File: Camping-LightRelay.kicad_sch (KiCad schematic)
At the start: 60 parts, among them CN1 U262-061N-4BVC11, CN2 XHP-2, CN3 B2B-XH-A, CN4 907-152A1022D10200, CN5 907-152A1022D10200, J1 J300, J2 J300, J3 J300, J4 J300, Q1 IRF7404, Q2 BC847, U1 LMV358ID

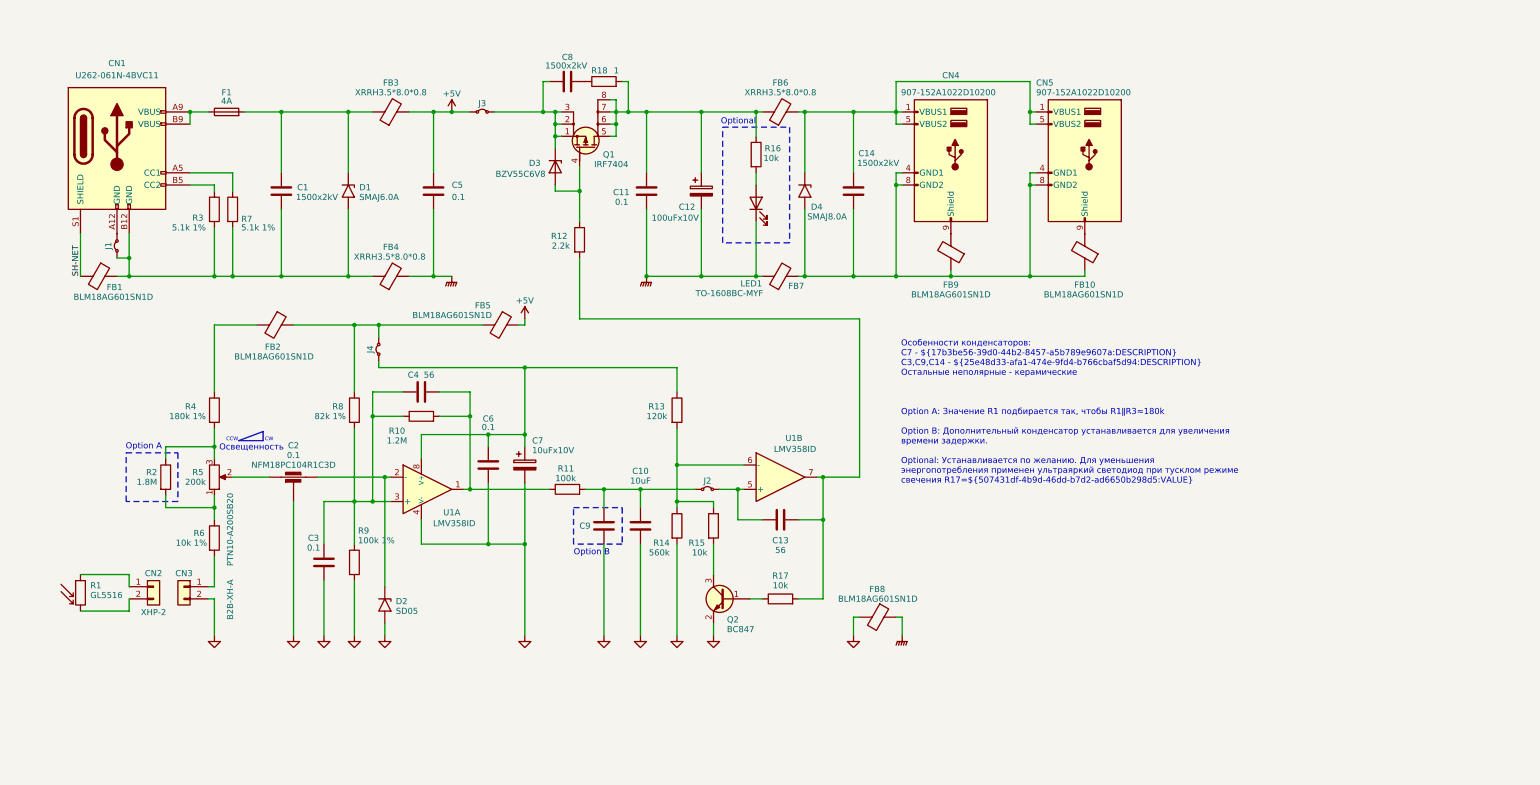
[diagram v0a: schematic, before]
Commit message: Отрисовка субмодуля управления питанием
Принципиальная схема (KiCAD) субмодуля управления PowerBank-ом. Создание электронных компонентов в базе. Выбор и назначение посадочных мест.
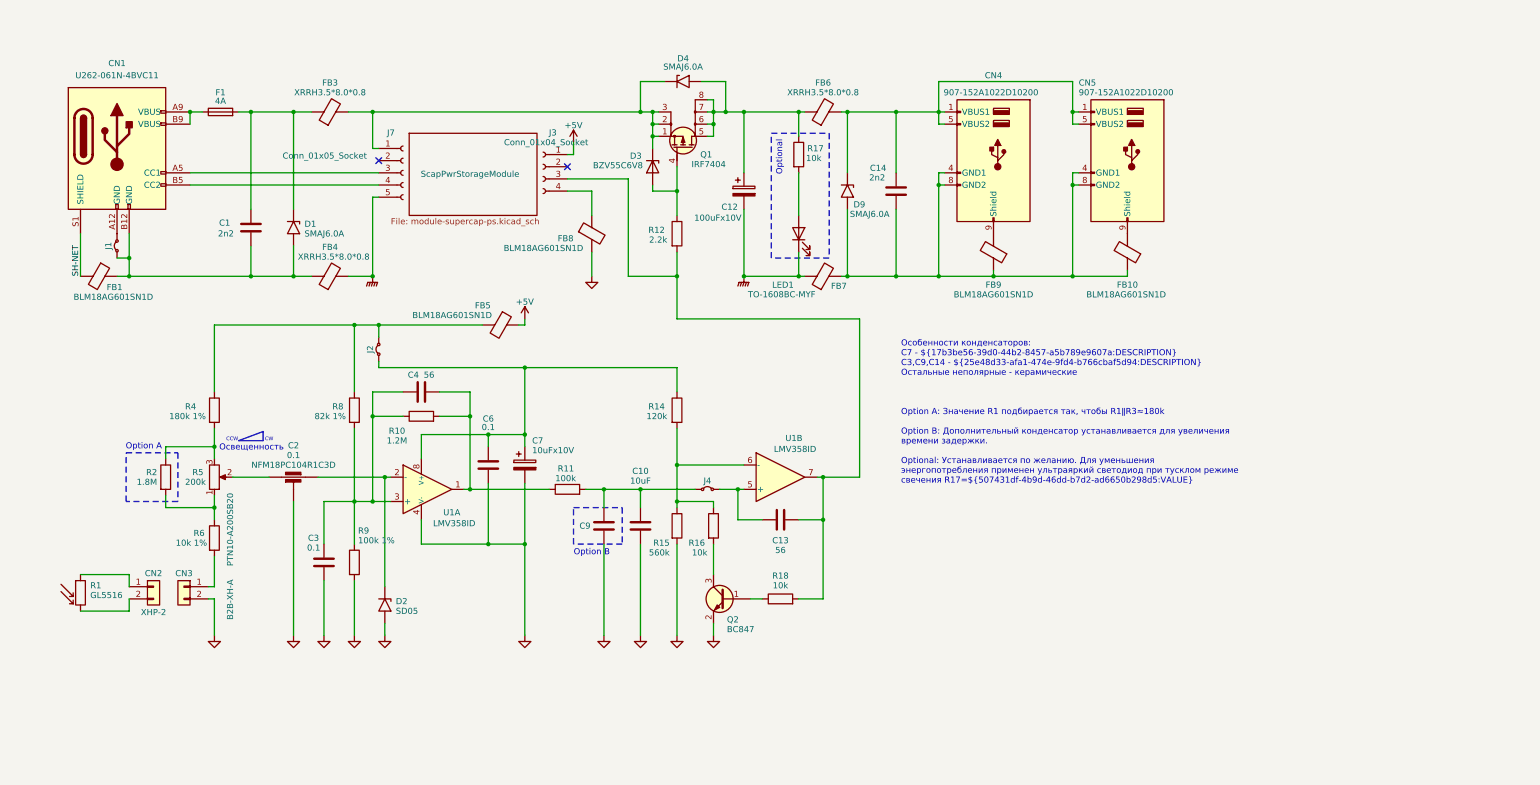
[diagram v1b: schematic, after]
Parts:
- removed C11, C5: 0.1, Capacitor_SMD:C_0603_1608Metric, symbol Device:C
- removed C8: 1500x2kV, Capacitor_THT:C_Disc_D7.5mm_W5.0mm_P5.00mm, symbol Device:C
- removed D4: SMAJ8.0A, Diode_SMD:D_SMA, symbol Diode:SMAJ8.0A
- removed FB2: BLM18AG601SN1D, Inductor_SMD:L_0603_1608Metric, symbol Device:FerriteBead
- removed J3: J300, lib:Junction_850mil, symbol Jumper:Jumper_2_Small_Bridged
- removed R18: 1, Resistor_SMD:R_0603_1608Metric, symbol Device:R
- removed R3, R7: 5.1k 1%, Resistor_SMD:R_0603_1608Metric, symbol Device:R
- added D4, D9: SMAJ6.0A, Diode_SMD:D_SMA, symbol Diode:SMAJ6.0A
- added J3: Conn_01x04_Socket, symbol Connector:Conn_01x04_Socket
- added J7: Conn_01x05_Socket, symbol Connector:Conn_01x05_Socket
- C1, C14: value 1500x2kV -> 2n2; footprint Capacitor_THT:C_Disc_D7.5mm_W5.0mm_P5.00mm -> Capacitor_THT:C_Disc_D8.0mm_W5.0mm_P7.50mm; Part Number (none) -> CY2222MD1PEE47J2A8
- C12: footprint Capacitor_THT:CP_Radial_D5.0mm_P2.50mm -> Capacitor_Tantalum_SMD:CP_EIA-3528-15_AVX-H_Pad1.50x2.35mm_HandSolder; Part Number (none) -> CA45-B010K107T
- C7: Part Number (none) -> TC212A106K010Y
- renumbered J4 to J2, J2 to J4, R13 to R14, R14 to R15, R15 to R16, R16 to R17, R17 to R18
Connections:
- net +5V: now also J3.1 (Pin_1); no longer FB3.2
- net GNDE: now also J7.5 (Pin_5); no longer FB8.1
- net at C14.1, CN4.1 (VBUS1), CN4.5 (VBUS2)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: now also D9.1 (A1)
- net at C14.2, CN4.4 (GND1), CN4.8 (GND2)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: now also D9.2 (A2)
- net at CN1.B5 (CC2): now also J7.4 (Pin_4)
- net at D3.1 (K), Q1.1 (S), Q1.2 (S)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: now also FB3.2, D4.1 (A1), J7.1 (Pin_1)
- net at CN1.A5 (CC1): now also J7.3 (Pin_3)
- net at FB5.2, J2.2 (B), R8.1: now also R4.1
- net at C12.1, FB6.1, Q1.5 (D)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: now also D4.2 (A2)
- net at C13.2, R12.2, R18.2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: now also J3.3 (Pin_3)
- new net: FB8.1, J3.4 (Pin_4)
- no-connect marks 0 -> 2
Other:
- added sheet ScapPwrStorageModule (module-supercap-ps.kicad_sch)
- moved on the sheet: C1, C12, C14, CN4, CN5, D1, D3, F1, FB10, FB3, FB4, FB6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

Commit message: Работа со схемой модуля
Частичная отрисовка и назначение посадочных мест субмодуля питания от PowerBank. *Работа продолжается*.
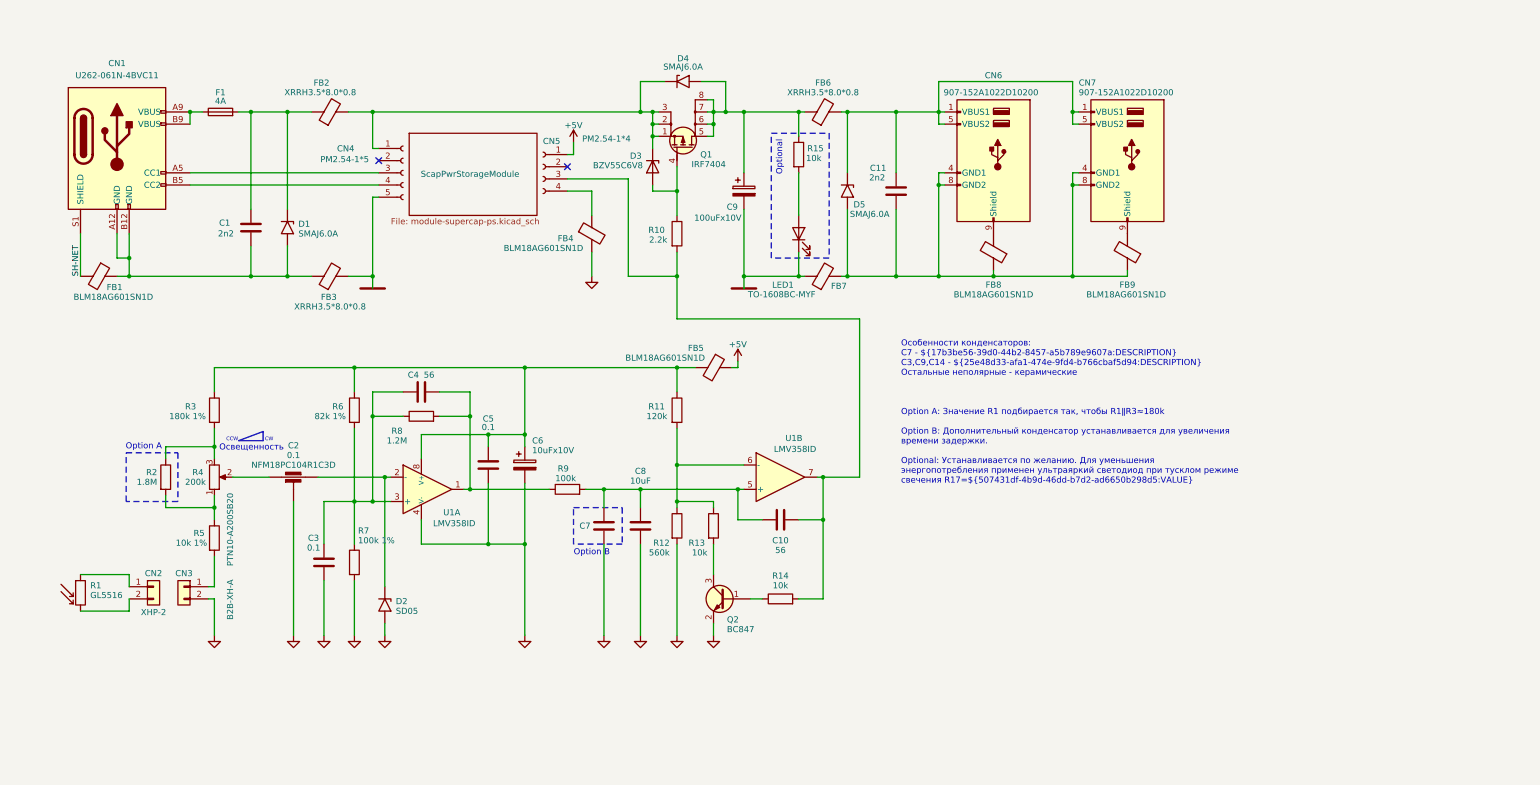
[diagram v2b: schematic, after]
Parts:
- removed J1: J300, lib:Junction_300mil, symbol Jumper:Jumper_2_Small_Bridged
- removed J2: J300, lib:Junction_400mil, symbol Jumper:Jumper_2_Small_Bridged
- removed J4: J300, lib:Junction_350mil, symbol Jumper:Jumper_2_Small_Bridged
- C2: Mfr. part NFM18PC104R1C3D -> (none); Part Number (none) -> NFM18PC104R1C3D
- CN4: renamed from J7; value Conn_01x05_Socket -> PM2.54-1*5; footprint (none) -> Connector_PinSocket_2.54mm:PinSocket_1x05_P2.54mm_Vertical
- CN5: renamed from J3; value Conn_01x04_Socket -> PM2.54-1*4; footprint (none) -> Connector_PinSocket_2.54mm:PinSocket_1x04_P2.54mm_Vertical
- R4: renamed from R5; Mfg. part PTN10-A200SB20 -> (none); Part Number (none) -> PTN10-A200SB20
- renumbered C13 to C10, C14 to C11, C6 to C5, C7 to C6, C9 to C7, C10 to C8, C12 to C9, CN4 to CN6, CN5 to CN7, D9 to D5, FB3 to FB2, FB4 to FB3, FB8 to FB4, FB9 to FB8, FB10 to FB9, R12 to R10, R14 to R11, R15 to R12, R16 to R13, R18 to R14, R17 to R15, R4 to R3, R6 to R5, R8 to R6, R9 to R7, R10 to R8, R11 to R9
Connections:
- net at C5.1, C6.1, R11.1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: now also FB5.2, R3.1, R6.1
- net at C1.2, CN1.B12 (GND), D1.2 (A2)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: now also CN1.A12 (GND)
- net at C10.1, U1.5 (+): now also C7.1, C8.1, R9.2
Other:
- moved on the sheet: D1, FB5

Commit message: Переделка топологии субмодулей
Фотореле вынесен в отдельный субмодуль, как дополнительная печатная плата. Схема управления PowerBank-ом перенесена на силовую плату с другими компонентами.
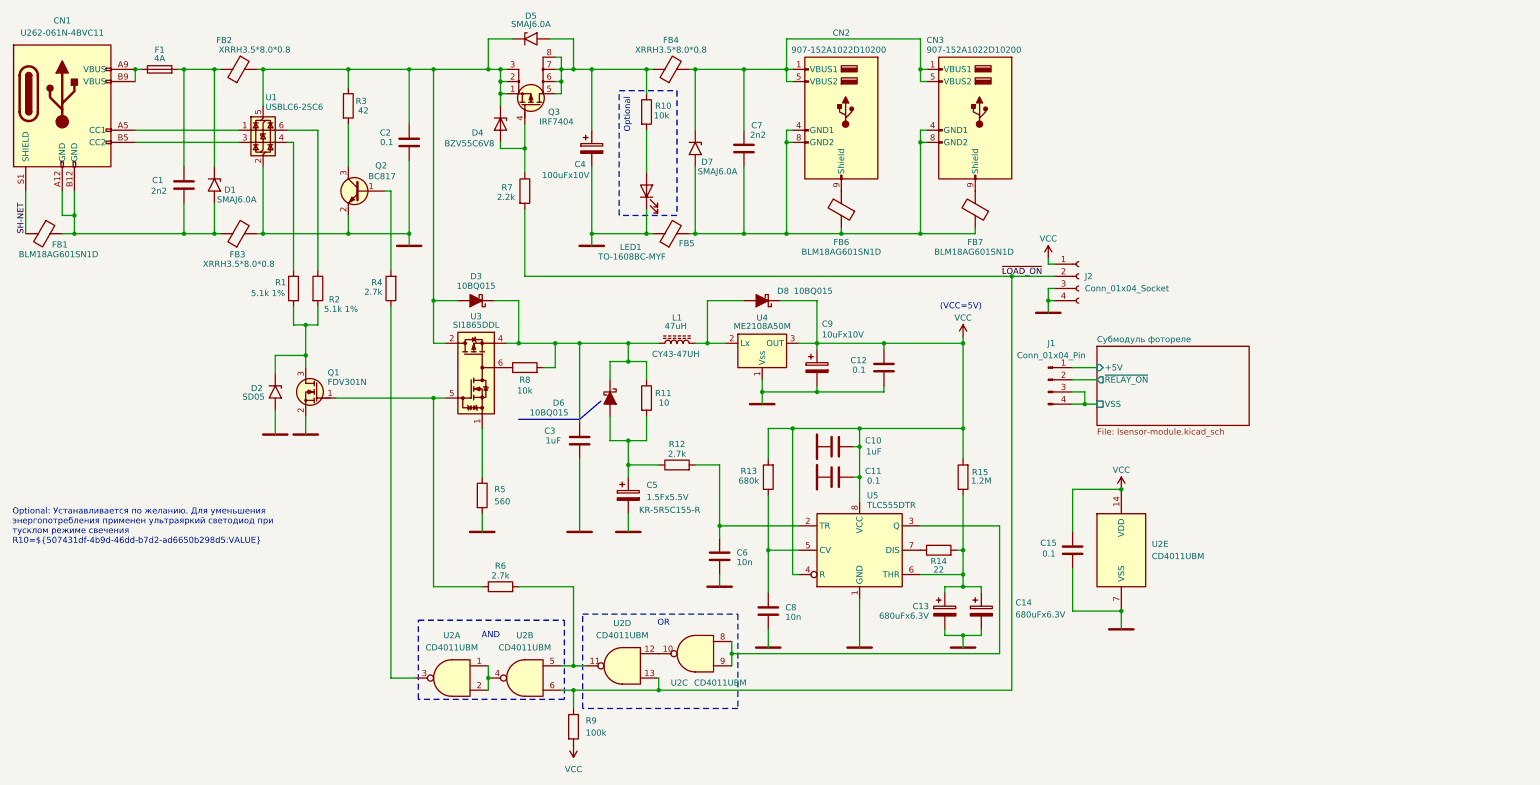
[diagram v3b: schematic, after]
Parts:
- removed C2: 0.1, lib:C_0603_3-terminal, symbol Device:Filter_EMI_C
- removed C4: 56, Capacitor_SMD:C_0603_1608Metric, symbol Device:C
- removed C5: 0.1, Capacitor_SMD:C_0603_1608Metric, symbol Device:C
- removed C6: 10uFx10V, Capacitor_Tantalum_SMD:CP_EIA-3216-10_Kemet-I_Pad1.58x1.35mm_HandSolder, symbol Device:C_Polarized
- removed C7: 10uF, Capacitor_SMD:C_0805_2012Metric, symbol Device:C
- removed CN2: XHP-2, symbol Connector_Generic:Conn_01x02
- removed CN3: B2B-XH-A, Connector_JST:JST_XH_B2B-XH-AM_1x02_P2.50mm_Vertical, symbol Connector_Generic:Conn_01x02
- removed CN4: PM2.54-1*5, Connector_PinSocket_2.54mm:PinSocket_1x05_P2.54mm_Vertical, symbol Connector:Conn_01x05_Socket
- removed CN5: PM2.54-1*4, Connector_PinSocket_2.54mm:PinSocket_1x04_P2.54mm_Vertical, symbol Connector:Conn_01x04_Socket
- removed FB4, FB5: BLM18AG601SN1D, Inductor_SMD:L_0603_1608Metric, symbol Device:FerriteBead
- removed Q2: BC847, Package_TO_SOT_SMD:SOT-23, symbol PCM_Transistor_BJT_AKL:BC847
- removed R1: GL5516, OptoDevice:R_LDR_5.1x4.3mm_P3.4mm_Vertical, symbol Sensor_Optical:LDR07
- removed R4: 200k, lib:TRIM_PTN10-A01HB20, symbol Device:R_Potentiometer
- removed R7: 100k 1%, Resistor_SMD:R_0603_1608Metric, symbol Device:R
- removed U1: LMV358ID, PCM_Package_SO_AKL:SO-8_3.9x4.9mm_P1.27mm, symbol PCM_Amplifier_Operational_AKL:LMV358ID
- added C11, C12, C15: 0.1, symbol Device:C
- added C13, C14: 680uFx6.3V, Capacitor_Tantalum_SMD:CP_EIA-7343-43_Kemet-X_Pad2.25x2.55mm_HandSolder, symbol Device:C_Polarized
- added C2: 0.1, Capacitor_SMD:C_0603_1608Metric, symbol Device:C
- added C5: 1.5Fx5.5V, symbol Device:C_Polarized
- added C6: 10n, symbol Device:C
- added C9: 10uFx10V, Capacitor_Tantalum_SMD:CP_EIA-3216-12_Kemet-S_Pad1.58x1.35mm_HandSolder, symbol Device:C_Polarized
- added D3, D6, D8: 10BQ015, Diode_SMD_AKL:D_SMB, symbol PCM_Diode_Schottky_AKL:VS-10BQ015
- added J1: Conn_01x04_Pin, symbol Connector:Conn_01x04_Pin
- added J2: Conn_01x04_Socket, symbol Connector:Conn_01x04_Socket
- added L1: 47uH, Inductor_SMD:L_Taiyo-Yuden_NR-50xx, symbol Device:L_Ferrite
- added Q1: FDV301N, Package_TO_SOT_SMD_AKL:SOT-23, symbol PCM_Transistor_MOSFET_AKL:FDV301N
- added Q2: BC817, Package_TO_SOT_SMD_AKL:SOT-23, symbol PCM_Transistor_BJT_AKL:BC817
- added R1: 5.1k 1%, PCM_Resistor_SMD_AKL:R_0603_1608Metric_Pad0.98x0.95mm, symbol Device:R
- added R15: 1.2M, PCM_Resistor_SMD_AKL:R_0603_1608Metric_Pad0.98x0.95mm, symbol Device:R
- added R4: 2.7k, PCM_Resistor_SMD_AKL:R_0603_1608Metric_Pad0.98x0.95mm, symbol Device:R
- added U1: USBLC6-2SC6, Package_TO_SOT_SMD:SOT-23-6, symbol Power_Protection:USBLC6-2SC6
- added U2: CD4011UBM, Package_SO:SOIC-14_3.9x8.7mm_P1.27mm, symbol 4xxx:4011
- added U3: SI1865DDL, Package_TO_SOT_SMD:SOT-363_SC-70-6, symbol LightRelay:SI1865DDL_R
- added U4: ME2108A50M, Package_TO_SOT_SMD:SOT-23-3, symbol LightRelay:ME2108A50M
- added U5: TLC555DTR, Package_SO:SOIC-8_3.9x4.9mm_P1.27mm, symbol Timer:TLC555xD
- C10: value 56 -> 1uF; footprint Capacitor_SMD:C_0603_1608Metric -> (none)
- C3: value 0.1 -> 1uF; footprint Capacitor_SMD:C_0603_1608Metric -> Capacitor_SMD:C_0805_2012Metric
- C8: value 10uF -> 10n; footprint Capacitor_SMD:C_0805_2012Metric -> (none)
- R11: value 120k -> 10; footprint Resistor_SMD:R_0603_1608Metric -> PCM_Resistor_SMD_AKL:R_0805_2012Metric_Pad1.15x1.40mm
- R12: value 560k -> 2.7k; footprint Resistor_SMD:R_0603_1608Metric -> PCM_Resistor_SMD_AKL:R_0603_1608Metric_Pad0.98x0.95mm
- R13: value 10k -> 680k; footprint Resistor_SMD:R_0603_1608Metric -> PCM_Resistor_SMD_AKL:R_0603_1608Metric_Pad0.98x0.95mm
- R14: value 10k -> 22; footprint Resistor_SMD:R_0603_1608Metric -> PCM_Resistor_SMD_AKL:R_0603_1608Metric_Pad0.98x0.95mm
- R2: value 1.8M -> 5.1k 1%; footprint Resistor_SMD:R_0603_1608Metric -> PCM_Resistor_SMD_AKL:R_0603_1608Metric_Pad0.98x0.95mm
- R3: value 180k 1% -> 42; footprint Resistor_SMD:R_0603_1608Metric -> PCM_Resistor_SMD_AKL:R_0805_2012Metric_Pad1.15x1.40mm
- R5: value 10k 1% -> 560; footprint Resistor_SMD:R_0603_1608Metric -> PCM_Resistor_SMD_AKL:R_0603_1608Metric_Pad0.98x0.95mm
- R6: value 82k 1% -> 2.7k; footprint Resistor_SMD:R_0603_1608Metric -> PCM_Resistor_SMD_AKL:R_0603_1608Metric_Pad0.98x0.95mm
- R8: value 1.2M -> 10k; footprint Resistor_SMD:R_0603_1608Metric -> PCM_Resistor_SMD_AKL:R_0603_1608Metric_Pad0.98x0.95mm
- R9: footprint Resistor_SMD:R_0603_1608Metric -> PCM_Resistor_SMD_AKL:R_0603_1608Metric_Pad0.98x0.95mm
- renumbered C9 to C4, C11 to C7, CN6 to CN2, CN7 to CN3, D3 to D4, D4 to D5, D5 to D7, FB6 to FB4, FB7 to FB5, FB8 to FB6, FB9 to FB7, Q1 to Q3, R15 to R10, R10 to R7
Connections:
- net GNDE: now also C3.2, C8.2, D2.2 (A2), R5.2, C12.1, C13.2, C14.2, C15.2, C2.2, C5.2, C6.2, C9.2, J2.3 (Pin_3), J2.4 (Pin_4), Q1.2 (S), Q2.2 (E), U1.2 (GND), U2.7 (VSS), U4.1 (Vss), U5.1 (GND)
- net at R5.1: now also U3.1; no longer R2.2
- net at R2.1: now also U1.6 (I/O1); no longer R3.2
- net at D4.1 (K), D5.1 (A1), FB2.2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: now also R3.1, C2.1, D3.2 (A), U1.5 (VBUS), U3.2 (D2), U3.3 (D2)
- net at R8.2: now also C3.1, R11.1, D3.1 (K), D6.1 (K), L1.1, U3.4 (S2); no longer R9.1
- net at D2.1 (A1): now also R2.2, Q1.3 (D), R1.2
- net at R14.1: now also U5.7 (DIS)
- net VCC: now reaches R13.2
- net VCC: now also C10.2, R9.2, C11.2, C12.2, C15.1, C9.1, D8.1 (K), J2.1 (Pin_1), R15.2, U2.14 (VDD), U4.3 (OUT), U5.4 (R), U5.8 (VCC)
- net at CN1.A5 (CC1): now also U1.1 (I/O1)
- net at CN1.B5 (CC2): now also U1.3 (I/O2)
- net at R11.2, R12.1: now also C5.1, D6.2 (A); no longer R13.1
- removed net GND: C3.2, C8.2, D2.2 (A2), R12.2
- new net: Q1.1 (G), R6.1, U3.5 (on/off)
- new net: R8.1, U3.6
- new net: R6.2, U2.11, U2.5
- new net: U2.10, U2.12
- new net: C13.1, C14.1, R14.2, R15.1, U5.6 (THR)
- new net: U2.1, U2.2, U2.4
- new net: R4.1, U2.3
- new net: C8.1, R13.1, U5.5 (CV)
- new net: C6.1, R12.2, U5.2 (TR)
- new net: Q2.1 (B), R4.2
- new net: Q2.3 (C), R3.2
- new net: R1.1, U1.4 (I/O2)
- new net: U2.8, U2.9, U5.3 (Q)
- new net: D8.2 (A), L1.2, U4.2 (Lx)
- new net GND2: C10.1, C11.1
- new net ~{LOAD_ON}: J2.2 (Pin_2), R7.2, R9.1, U2.13, U2.6
- new net Субмодуль фотореле/+5V: J1.1 (Pin_1)
- new net Субмодуль фотореле/VSS: J1.3 (Pin_3), J1.4 (Pin_4)
- new net Субмодуль фотореле/~{RELAY_ON}: J1.2 (Pin_2)
- no-connect marks 2 -> 0
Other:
- removed sheet ScapPwrStorageModule
- added sheet Субмодуль фотореле (lsensor-module.kicad_sch)
- note added: "(VCC=5V)"
- note added: "AND"
- note added: "OR"
- note removed: "CCW"
- note removed: "CW"
- note removed: "Option A"
- note removed: "Option B"
- note removed: "Освещенность"
- moved on the sheet: C1, C4, C7, CN1, CN2, CN3, D1, D4, D5, D7, F1, FB1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
